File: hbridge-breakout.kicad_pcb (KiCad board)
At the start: 2 copper layers, 28.5 x 38.6 mm, 15 parts, among them J1 Conn_01x10, J2 Conn_01x04, J3 Conn_01x08, U1 74HC00, U2 DRV8870DDA

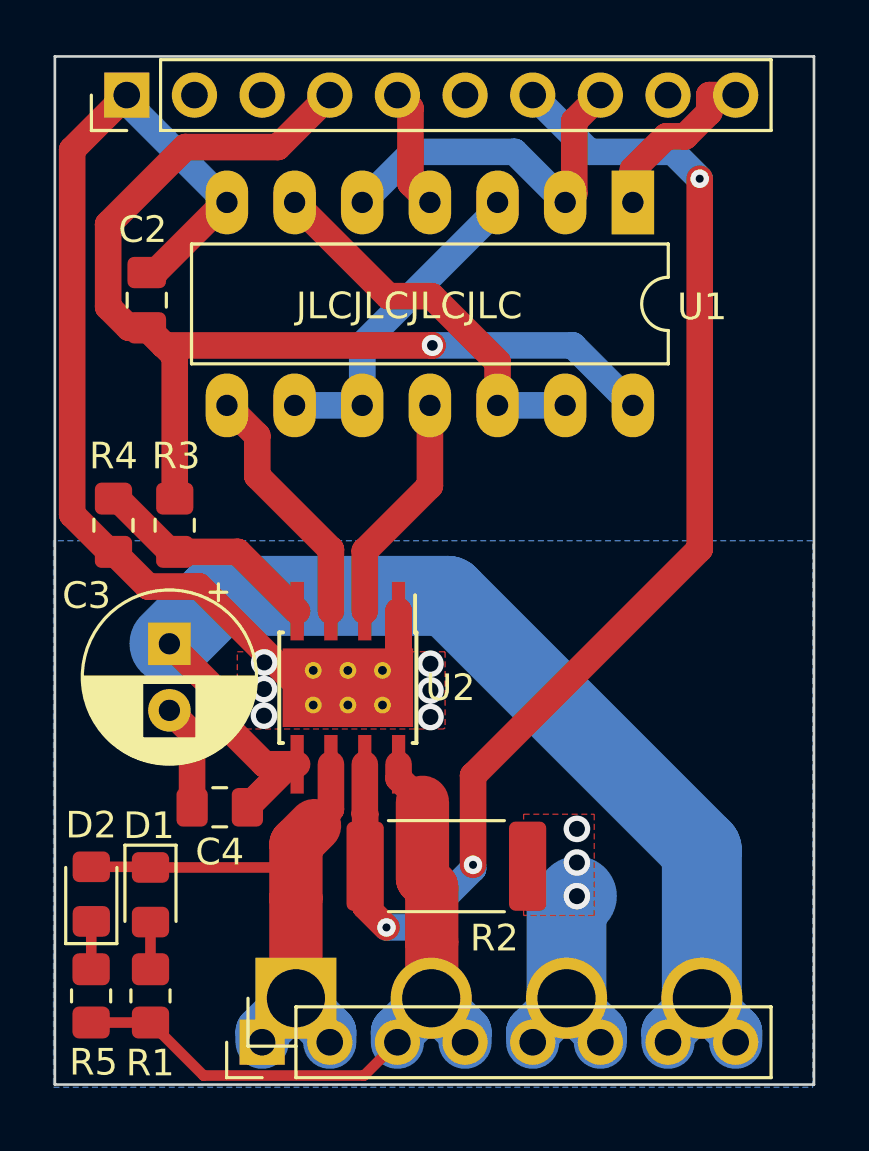
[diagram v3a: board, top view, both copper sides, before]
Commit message: Heap of rework to make power tracks simpler, and caps closer to chip.
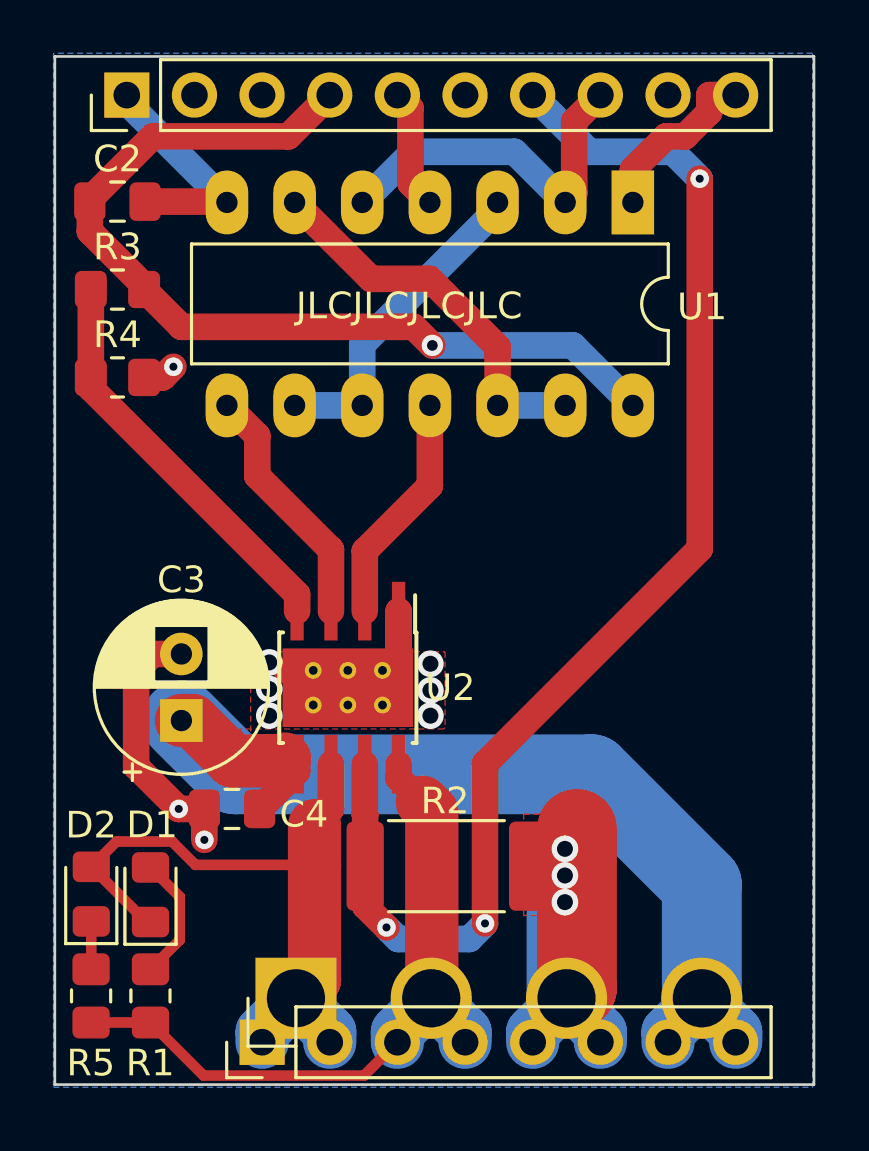
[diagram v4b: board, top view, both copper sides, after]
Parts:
- moved R3 9.11 mm to (152.9, 84.5), turned to 180 degrees
- moved R4 5.55 mm to (152.9, 87.8), turned to 0 degrees
- moved C2 3.86 mm to (152.9, 81.2), turned to 0 degrees
- moved C3 2.92 mm to (155.3, 100.7), turned to 90 degrees
- moved C4 0.46 mm to (157.2, 104.0)
- turned D1 to 90 degrees
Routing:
- net GND: track 61.7 -> 44.4 mm, vias 9 -> 12
- net Net-(U2-VREF): track 8.65 -> 15.3 mm
- net VCC: track 44.1 -> 37.5 mm
- net VDD: track 41.5 -> 35.0 mm
- net /OUTA: track 21.8 -> 25.9 mm
- net Net-(D1-A): track 1.77 -> 4.73 mm
- net /CS: track 47.6 -> 49.5 mm
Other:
- board text added: "mjd 1.2a 19-Sep-23"
- board text removed: "mjd 1.1a 16-Aug-23"
